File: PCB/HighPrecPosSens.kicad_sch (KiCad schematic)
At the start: 37 parts

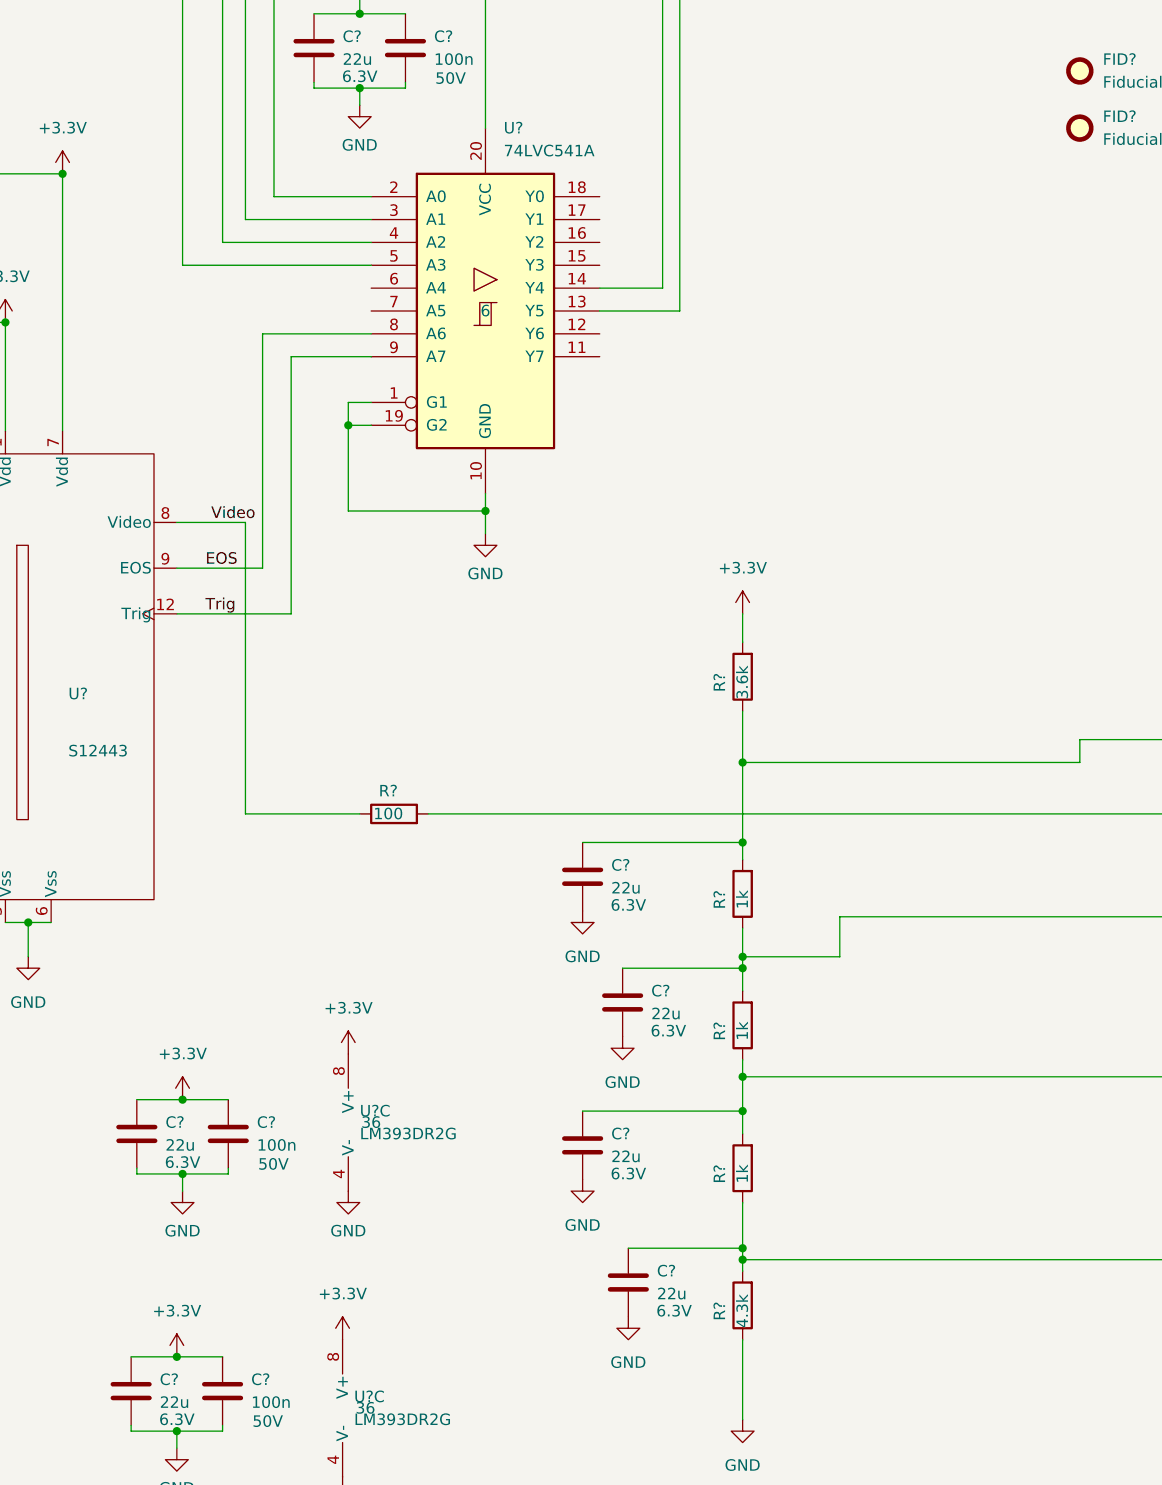
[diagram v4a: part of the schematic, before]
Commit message: added some wires and simulation of lt1818
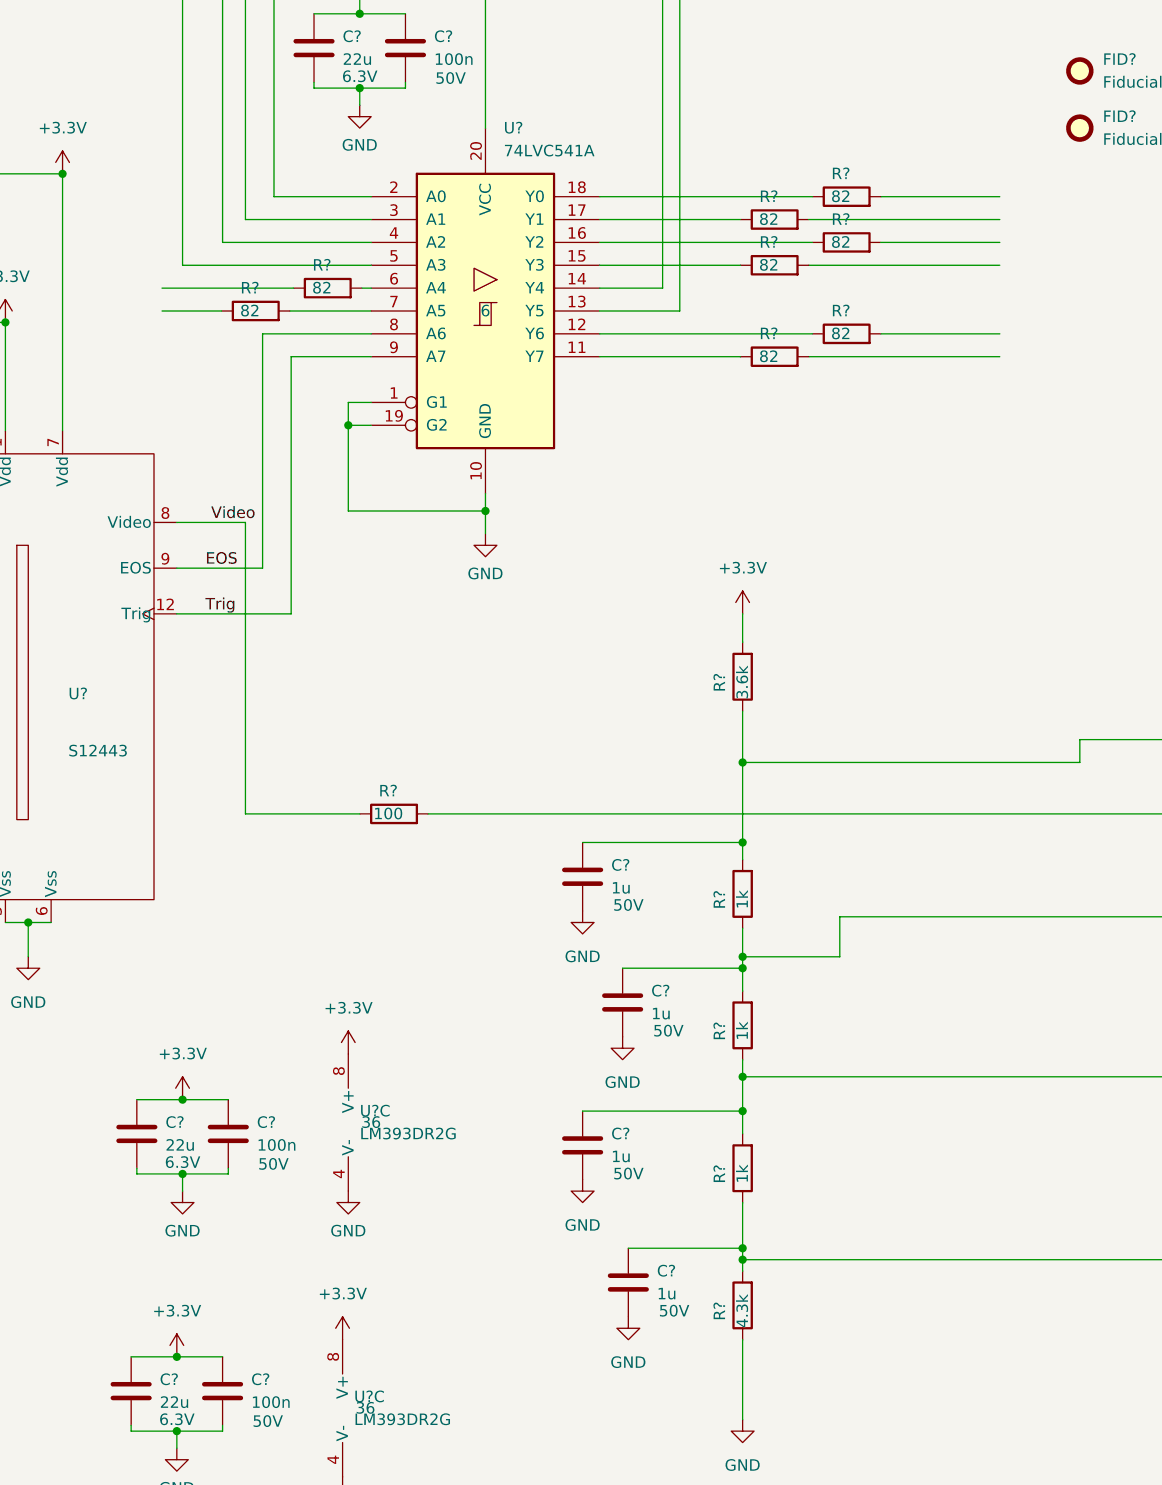
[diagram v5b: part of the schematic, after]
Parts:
- removed C? (x3): 22u, Capacitor_SMD:C_0603_1608Metric, symbol Device:C
- added C? (x3): 1u, Capacitor_SMD:C_0603_1608Metric, symbol Device:C
- added R? (x8): 82, Resistor_SMD:R_0603_1608Metric, symbol Device:R
- C?: value 22u -> 1u; ManufacturerPartNum CL10A226MQ8NRNC -> CL10A105KB8NNNC; SourcingPartNum C59461 -> C15849; Umax 6.3V -> 50V
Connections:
- net GND: now also C?.2, C?.2, C?.2
- net at R?.1, R?.2, U?.2 (-): now also C?.1 (x2)
- net at R?.1, R?.2, U?.6 (-): now also C?.1
- net at U?.11 (Y7): now also R?.1
- net at U?.12 (Y6): now also R?.1
- net at U?.15 (Y3): now also R?.1
- net at U?.16 (Y2): now also R?.1
- net at U?.17 (Y1): now also R?.1
- net at U?.18 (Y0): now also R?.1
- net at U?.6 (A4): now also R?.2
- net at U?.7 (A5): now also R?.2

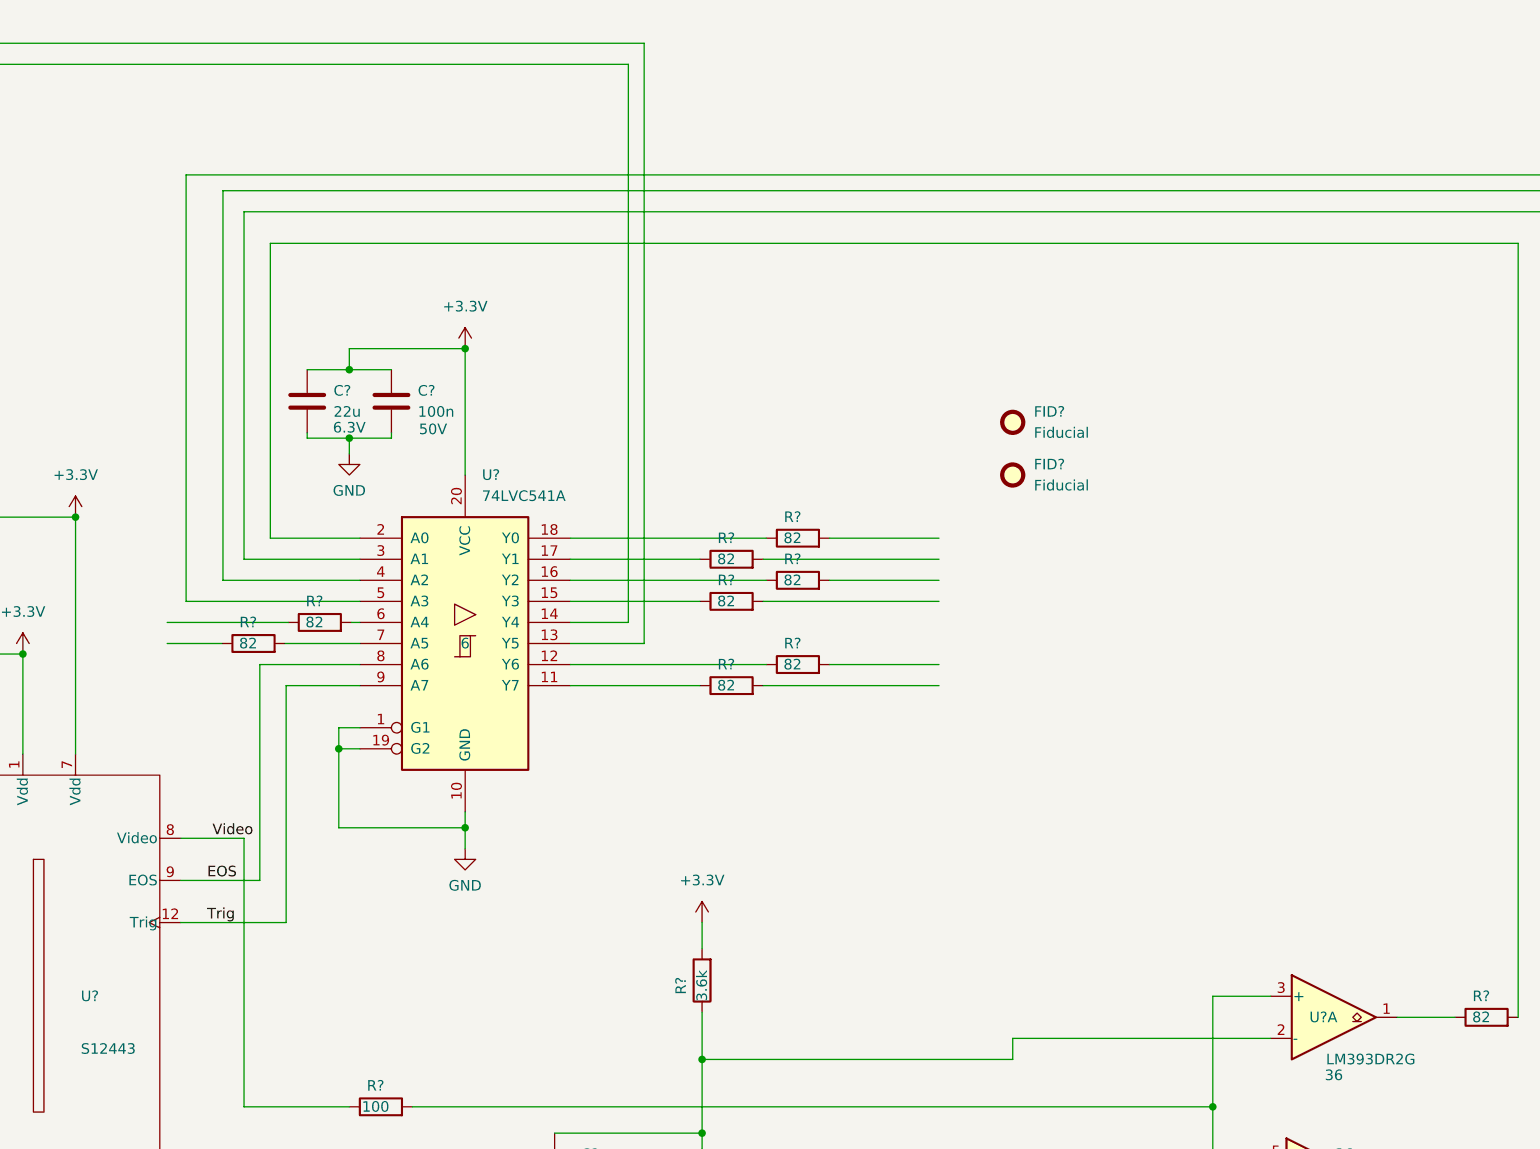
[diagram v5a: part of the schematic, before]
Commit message: added pico to schematic
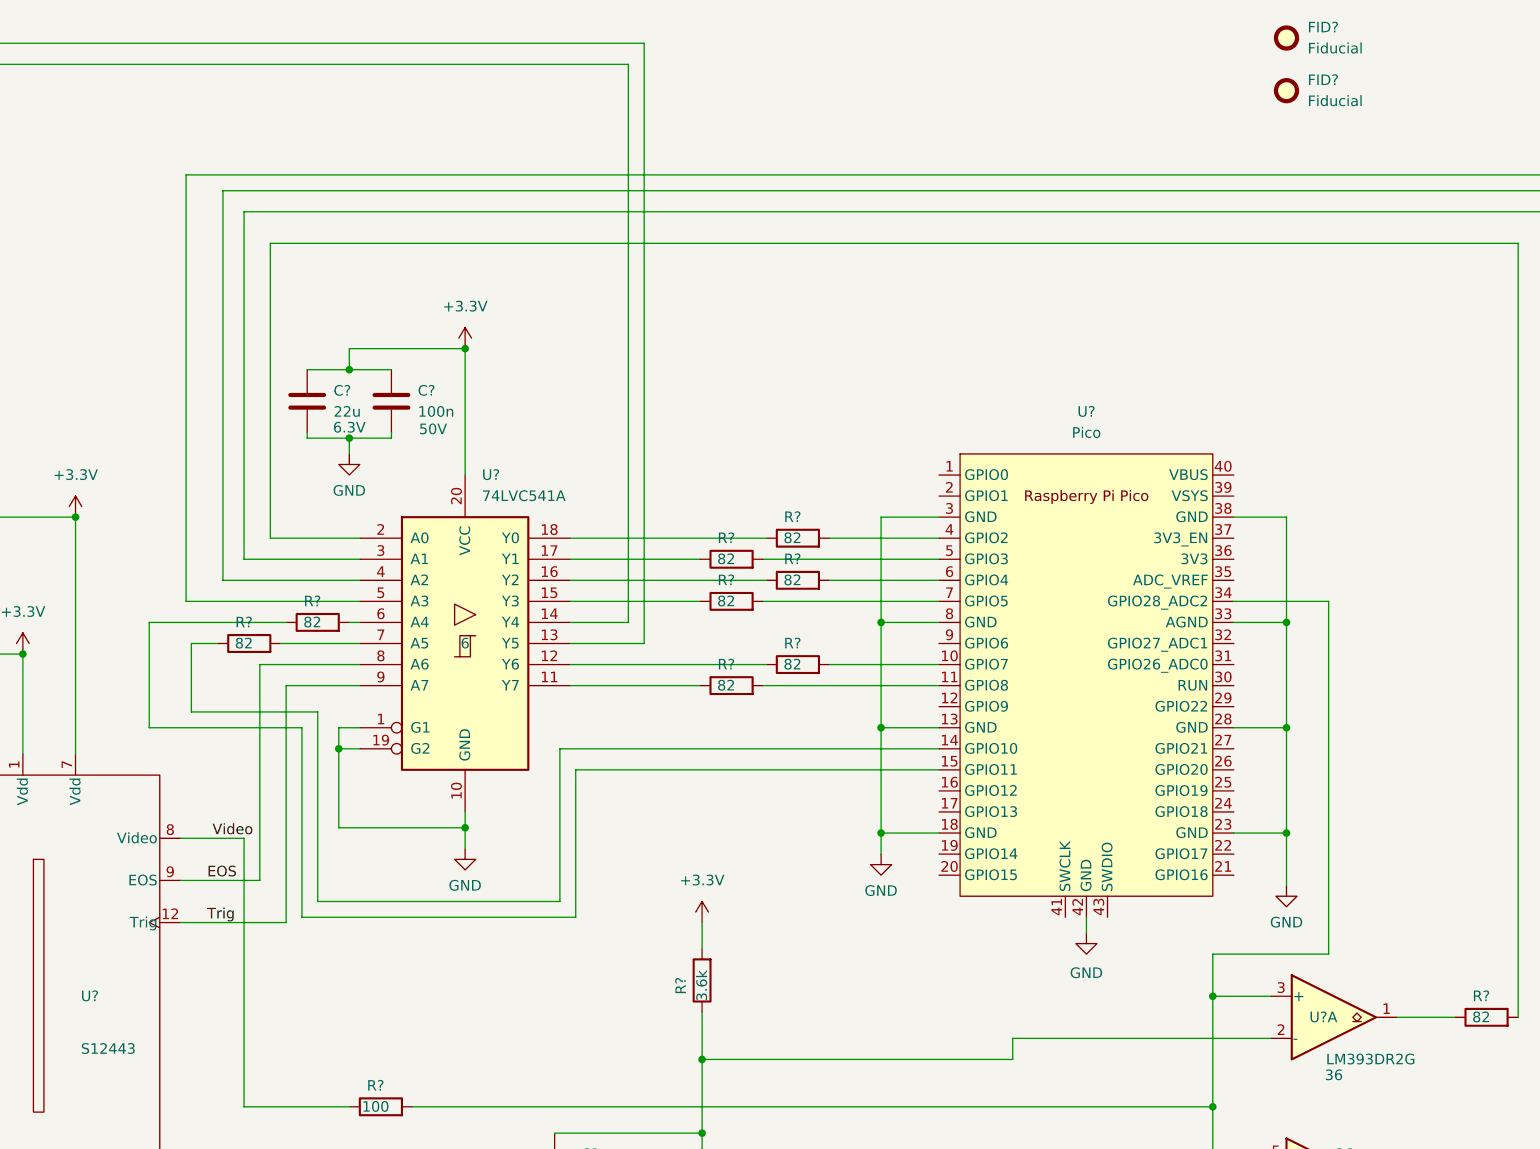
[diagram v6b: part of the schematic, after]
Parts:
- added U?: Pico, Pico:RPi_Pico_SMD_TH, symbol Pico:Pico
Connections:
- net GND: now also U?.13 (GND), U?.18 (GND), U?.23 (GND), U?.28 (GND), U?.3 (GND), U?.33 (AGND), U?.38 (GND), U?.42 (GND), U?.8 (GND)
- net at R?.2: now also U?.10 (GPIO7)
- net at R?.2, U?.3 (+), U?.3 (+)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: now also U?.34 (GPIO28_ADC2)
- net at R?.1: now also U?.14 (GPIO10)
- net at R?.2: now also U?.6 (GPIO4)
- net at R?.1: now also U?.15 (GPIO11)
- net at R?.2: now also U?.5 (GPIO3)
- net at R?.2: now also U?.11 (GPIO8)
- net at R?.2: now also U?.4 (GPIO2)
- net at R?.2: now also U?.7 (GPIO5)
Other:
- moved on the sheet: FID?, R?
